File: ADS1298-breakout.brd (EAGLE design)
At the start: 63.5 x 25.4 mm, 31 parts, among them IC1 ADS1298*PAG*, IC2 TPS73250DBVT, IC3 TPS73233DBVT

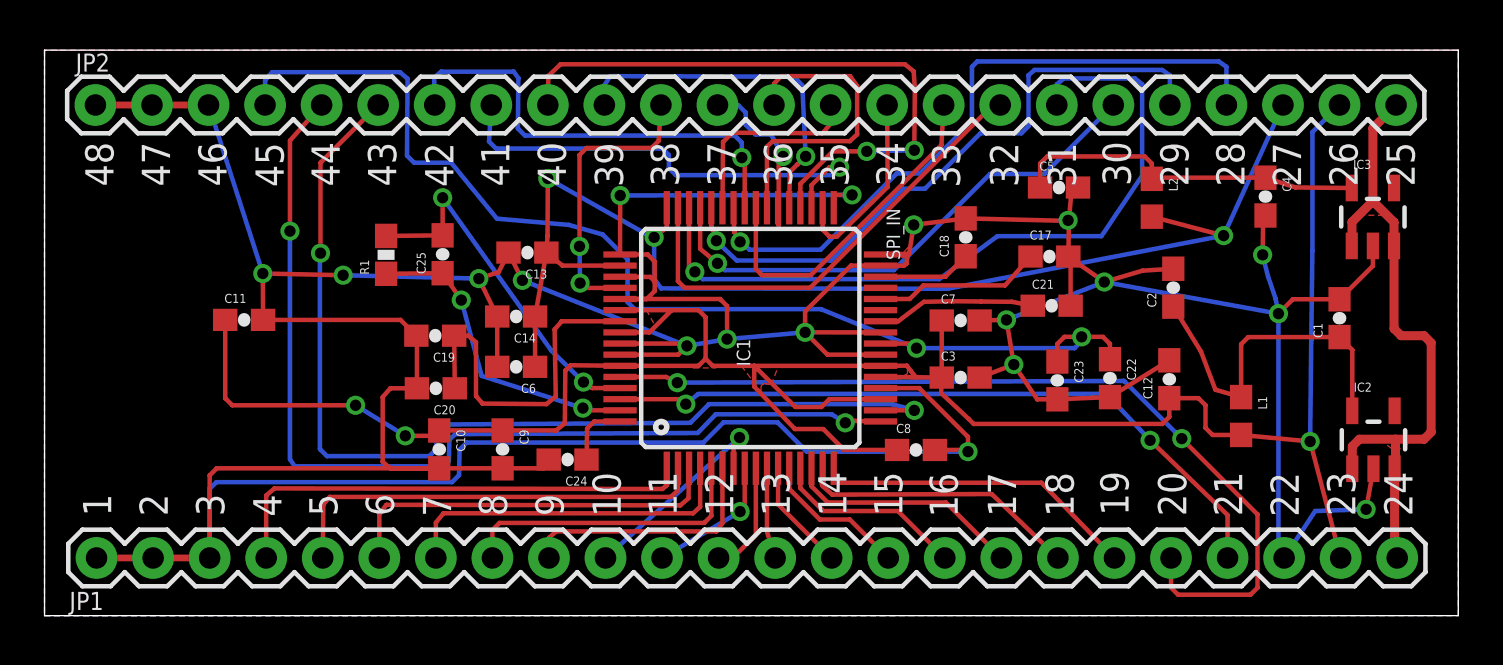
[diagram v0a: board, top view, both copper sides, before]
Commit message: top silkscreen has pin numbers and functions; board name and version; OSH logo; and CC-BY-SA license
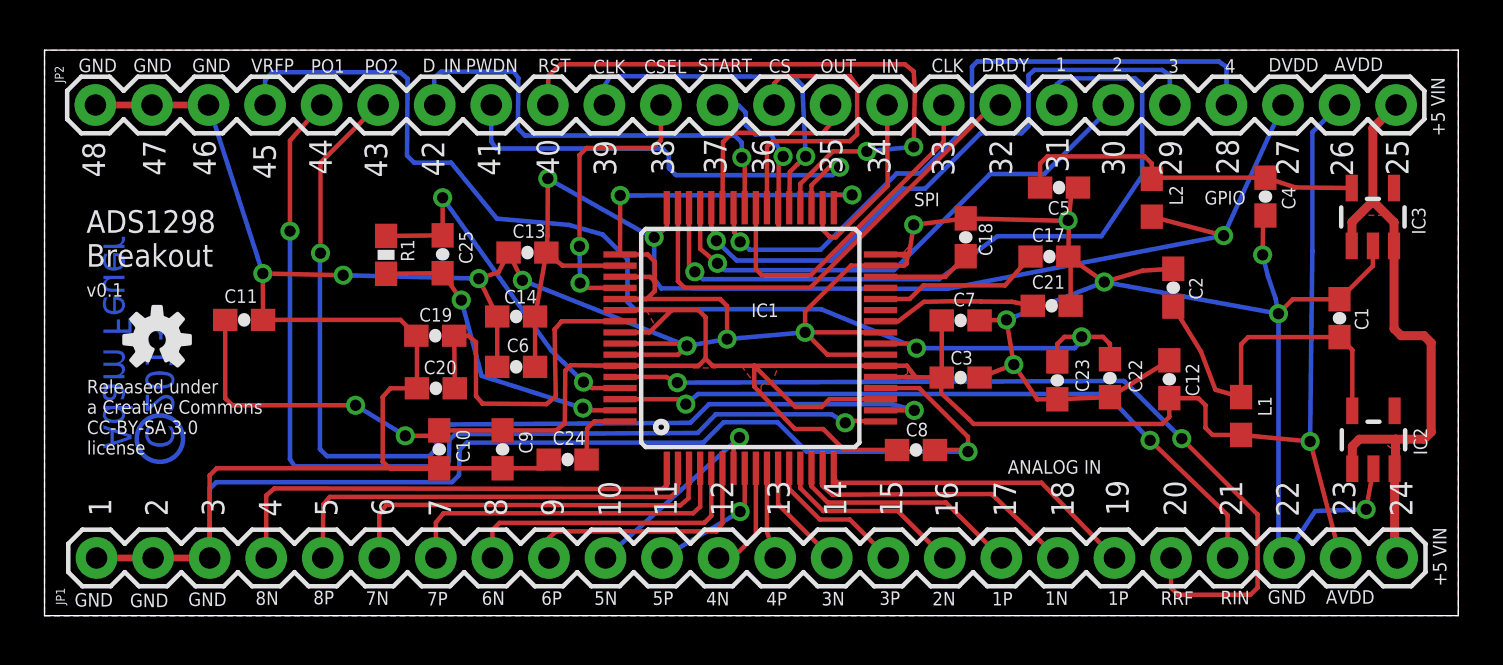
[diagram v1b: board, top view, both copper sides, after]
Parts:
- added U$1: (no value), SparkFun-Aesthetics:OSHW-LOGO-S
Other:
- board text added: "+5 VIN"
- board text added: "1N"
- board text added: "1P"
- board text added: "2N"
- board text added: "3N"
- board text added: "3P"
- board text added: "4N"
- board text added: "4P"
- board text added: "5N"
- board text added: "5P"
- board text added: "6N"
- board text added: "6P"
- board text added: "7N"
- board text added: "7P"
- board text added: "8N"
- board text added: "8P"
- board text added: "ADS1298 Breakout"
- board text added: "ANALOG IN"
- board text added: "AVDD"
- board text added: "C 2013 Adam Feuer"
- board text added: "CLK"
- board text added: "CS"
- board text added: "CSEL"
- board text added: "DRDY"
- board text added: "DVDD"
- board text added: "D_IN"
- board text added: "GND"
- board text added: "GPIO"
- board text added: "IN"
- board text added: "OUT"
- board text added: "PO1"
- board text added: "PO2"
- board text added: "PWDN"
- board text added: "RIN"
- board text added: "RRF"
- board text added: "RST"
- board text added: "Released under a Creative Commons CC-BY-SA 3.0 license"
- board text added: "SPI"
- board text added: "START"
- board text added: "VRFP"
- board text added: "v0.1"
- board text removed: "ADS1298 Breakout v0.1"
- board text removed: "SPI_IN"
